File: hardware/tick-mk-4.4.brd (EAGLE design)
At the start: 96 x 53 mm, 36 parts, among them IC1 ATMEGA328P, IC2 DS1338, IC3 L7805, Y1 16MHz

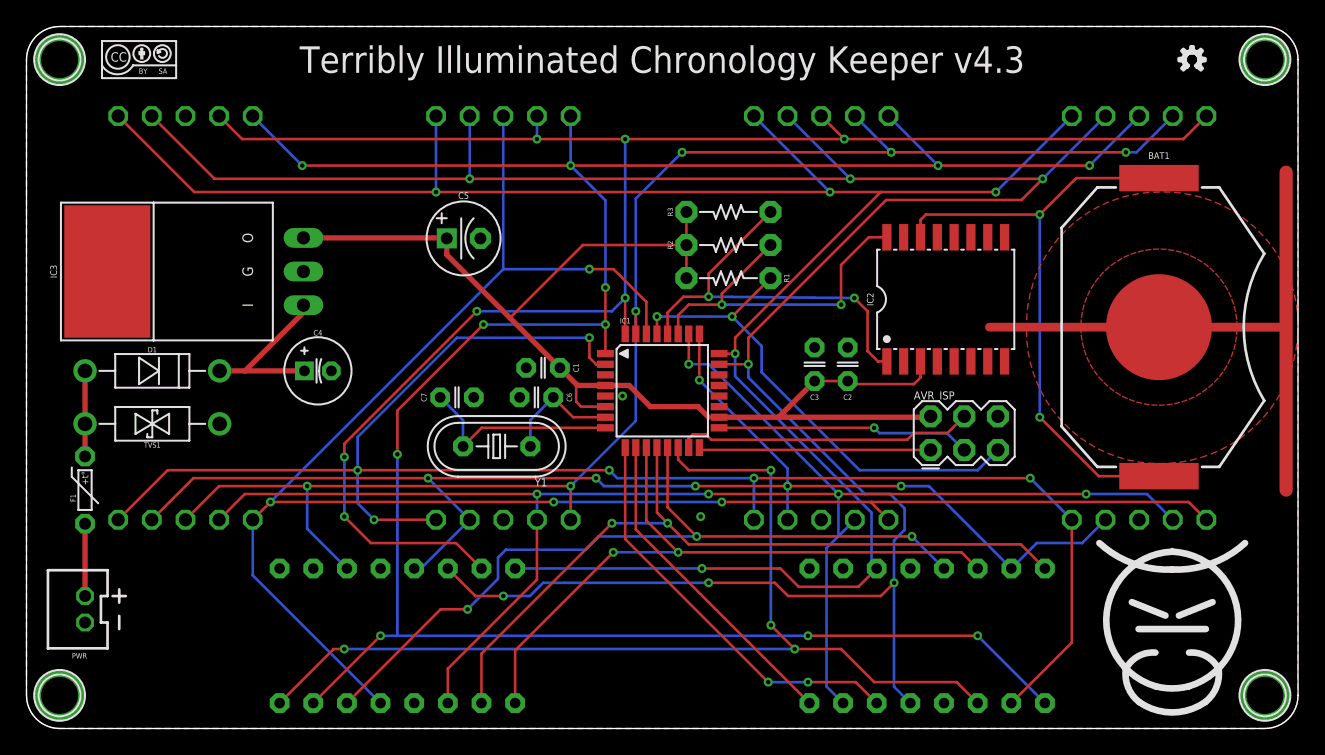
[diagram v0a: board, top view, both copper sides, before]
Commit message: pth version done, way easier than expected
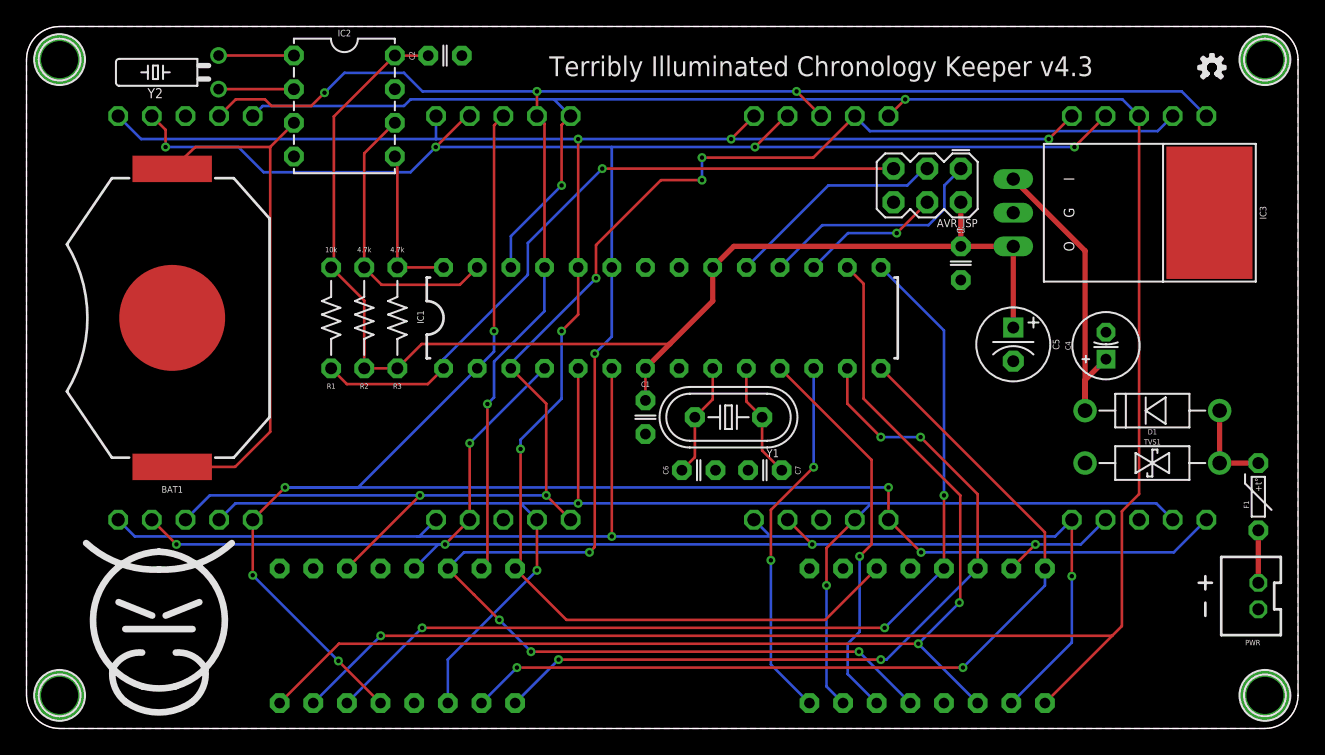
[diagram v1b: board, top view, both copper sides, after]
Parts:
- removed U$1, U$2: (no value), A_butts:CC-BY-SA-4.0-NO-URL
- added Y2: 32.768kHz, A_butts:TC26H
- IC1: device A_butts:TQFP32-08 -> A_butts:DIL28-3
- IC2: value DS1338 -> DS1307; device A_butts:SO16W -> A_butts:DIL08
- R1, R2, R3: device A_butts:RESISTOR-AXIAL-PTH-6.35MM -> A_butts:RESISTOR-AXIAL-PTH-7.62MM
- moved PWR 88.6 mm to (93.0, 10.0)
- moved F1 88.6 mm to (93.0, 17.5)
- moved U$4 88.0 mm to (4.00, 10.0)
- moved U$3 76.5 mm to (10.0, 7.00)
- moved D1 75.6 mm to (85.0, 24.0), turned to 180 degrees
- moved TVS1 75.6 mm to (85.0, 20.0), turned to 0 degrees
- moved BAT1 74.5 mm to (11.0, 31.0), turned to 180 degrees
- moved IC3 61.4 mm to (78.3, 38.9), turned to 270 degrees
- moved C4 59.5 mm to (81.5, 28.9), turned to 90 degrees
- moved IC2 47.7 mm to (24.0, 47.0), turned to 270 degrees
- moved C5 42.3 mm to (74.5, 29.0), turned to 270 degrees
- moved C2 38.3 mm to (31.6, 50.8), turned to 0 degrees
- moved R1 30.1 mm to (23.0, 31.0), turned to 90 degrees
- moved R2 28.0 mm to (25.5, 31.0), turned to 90 degrees
- moved R3 26.2 mm to (28.0, 31.0), turned to 90 degrees
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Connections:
- new net N$2: IC2.1, Y2.2
- new net N$3: IC2.2, Y2.1
- net A2: now also DIGIT1.9, DIGIT2.9, DIGIT3.8, DIGIT4.10, DISPLAY2.15; no longer DIGIT1.4, DIGIT2.4, DIGIT3.4, DIGIT4.4, DISPLAY1.15, DISPLAY2.13
- net A3: now also DIGIT1.10, DIGIT2.10, DIGIT3.10, DIGIT4.8, DISPLAY1.1, DISPLAY2.7; no longer DIGIT1.2, DIGIT2.2, DIGIT3.2, DIGIT4.2, DISPLAY1.7, DISPLAY2.3
- net D0: now also IC1.2; no longer IC1.30
- net D1: now also IC1.3; no longer IC1.31
- net D10: now also IC1.16; no longer IC1.14
- net D11/MOSI: now also IC1.17; no longer IC1.15
- net D12/MISO: now also IC1.18; no longer IC1.16
- net D13/SCK: now also IC1.19; no longer IC1.17
- net D2: now also DIGIT1.4, DIGIT2.4, DIGIT3.4, DIGIT4.4, DISPLAY1.15, DISPLAY2.13, IC1.4; no longer DIGIT1.9, DIGIT2.9, DIGIT3.8, DIGIT4.10, DISPLAY2.15, IC1.32
- net D3: now also DIGIT1.2, DIGIT2.2, DIGIT3.2, DIGIT4.2, DISPLAY1.7, DISPLAY2.3, IC1.5; no longer DIGIT1.10, DIGIT2.10, DIGIT3.10, DIGIT4.8, DISPLAY1.1, DISPLAY2.7, IC1.1
- net D4: now also IC1.6; no longer IC1.2
- net D5: now also IC1.11; no longer IC1.9
- net D6: now also IC1.12; no longer IC1.10
- net D7: now also IC1.13; no longer IC1.11
- net D8: now also IC1.14; no longer IC1.12
- net D9: now also IC1.15; no longer IC1.13
- net GND: now also IC1.22, IC1.8; no longer IC1.21, IC1.3, IC1.5, IC2.10, IC2.11, IC2.12, IC2.13, IC2.15, IC2.5, IC2.6, IC2.7, IC2.8, IC2.9
- net N$1: now also IC2.3; no longer IC2.14
- net N$6: now also IC1.9, Y1.2; no longer IC1.7, Y1.1
- net N$9: now also IC1.10, Y1.1; no longer IC1.8, Y1.2
- net RST: now also IC1.1; no longer IC1.29
- net SCL: now also IC2.5; no longer IC2.1
- net SDA: now also IC2.6; no longer IC2.16
- net VCC: now also IC1.20, IC1.7, IC2.8; no longer IC1.18, IC1.4, IC1.6, IC2.3
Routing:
- net D3: track 189.2 -> 118.6 mm, vias 11 -> 3
- net A3: track 128.3 -> 194.5 mm, vias 5 -> 3
- net GND: track 46.3 -> 0.00 mm, vias 2 -> 0
- net D2: track 138.1 -> 97.9 mm, vias 7 -> 5
- net D4: track 128.9 -> 105.0 mm, vias 6 -> 2
- net A0: track 187.0 -> 164.9 mm, vias 7 -> 9
- net SCL: track 30.7 -> 11.9 mm, vias 2 -> 0
- net A1: track 157.7 -> 142.5 mm
- net D9: track 59.8 -> 74.0 mm
- net A2: track 104.6 -> 118.5 mm, vias 6 -> 4
- net RST: track 37.7 -> 51.5 mm, vias 2 -> 1
- net D11/MOSI: track 22.5 -> 10.6 mm, vias 0 -> 1
- net D10: track 78.6 -> 89.7 mm, vias 4 -> 2
- net N$8: track 13.2 -> 24.3 mm
- net D0: track 143.5 -> 133.4 mm, vias 4 -> 6
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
